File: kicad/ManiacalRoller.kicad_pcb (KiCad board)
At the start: 2 copper layers, 69.5 x 71 mm, 37 parts, among them CON1 AVR-ISP-6, IC1 ATMEGA328P-P, Q1 Q_NPN_EBC, Q2 Q_NPN_EBC, SW1 BTN_coin, SW2 BTN_d4, SW3 BTN_d6, SW4 BTN_d8, SW5 BTN_d10, SW6 BTN_d12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

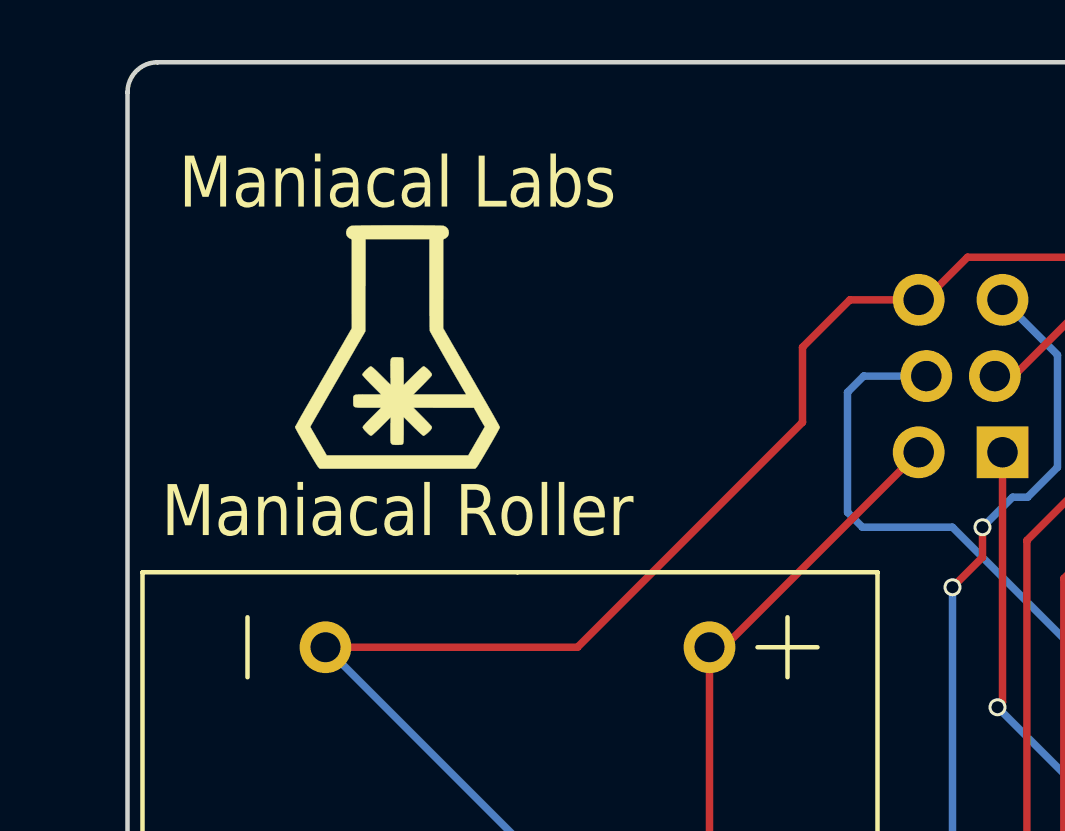
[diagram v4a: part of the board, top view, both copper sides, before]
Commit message: Tweaked logo size/position
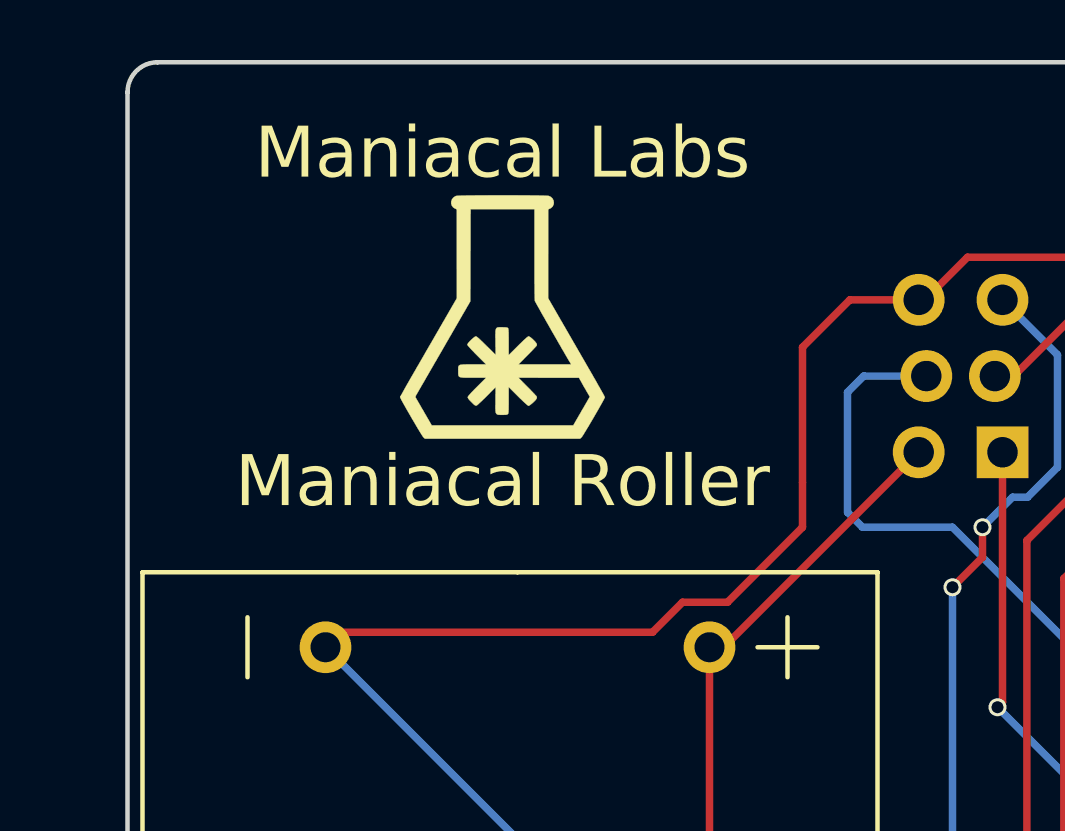
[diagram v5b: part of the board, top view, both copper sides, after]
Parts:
- moved G*** 3.64 mm to (100.0, 50.0)
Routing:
- net GND: track 245.0 -> 247.0 mm
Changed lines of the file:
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@@
     (thickness 1.6)
     (drawings 19)
-    (tracks 364)
+    (tracks 368)
     (zones 0)
     (modules 37)
@@
   )
   (module mod:logo_MLlabs_small (layer F.Cu)
-    (at 96.5 51)
+    (at 100 50)
     (fp_text reference G*** (at 0 0) (layer F.SilkS) hide
       (effects (font (thickness 0.3)))
@@
   (gr_arc (start 88.5 42.5) (end 87.5 42.5) (angle 90) (layer Edge.Cuts) (width 0.15))
   (gr_arc (start 156 111.5) (end 157 111.5) (angle 90) (layer Edge.Cuts) (width 0.15))
-  (gr_text "Maniacal Labs\n\n\n\nManiacal Roller" (at 96.5 51) (layer F.SilkS)
-    (effects (font (size 1.7 1.5) (thickness 0.3)))
+  (gr_text "Maniacal Labs\n\n\n\nManiacal Roller" (at 100 50) (layer F.SilkS)
+    (effects (font (size 1.7 1.7) (thickness 0.3)))
   )
   (gr_text 100 (at 154.5 84 90) (layer F.SilkS)
@@
   (segment (start 130 107) (end 130 109.5) (width 0.25) (layer B.Cu) (net 1))
   (segment (start 130.38 106.62) (end 130 107) (width 0.25) (layer B.Cu) (net 1))
+  (segment (start 94.6 60.5) (end 105 60.5) (width 0.25) (layer F.Cu) (net 2))
+  (segment (start 105 60.5) (end 106 59.5) (width 0.25) (layer F.Cu) (net 2))
+  (segment (start 106 59.5) (end 107.5 59.5) (width 0.25) (layer F.Cu) (net 2))
+  (segment (start 107.5 59.5) (end 110 57) (width 0.25) (layer F.Cu) (net 2))
+  (segment (start 110 57) (end 110 55.5) (width 0.25) (layer F.Cu) (net 2))
+  (segment (start 111.58 49.42) (end 113.873 49.42) (width 0.25) (layer F.Cu) (net 2))
+  (segment (start 110 51) (end 111.58 49.42) (width 0.25) (layer F.Cu) (net 2))
+  (segment (start 110 55.5) (end 110 51) (width 0.25) (layer F.Cu) (net 2))
+  (segment (start 94.6 60.5) (end 94.1 61) (width 0.25) (layer F.Cu) (net 2))
   (segment (start 120 81.5) (end 119.5 81.5) (width 0.25) (layer B.Cu) (net 2))
   (segment (start 119.5 81.5) (end 118 80) (width 0.25) (layer B.Cu) (net 2))
+  (segment (start 118 80) (end 113.1 80) (width 0.25) (layer B.Cu) (net 2))
   (segment (start 113.1 80) (end 94.1 61) (width 0.25) (layer B.Cu) (net 2))
-  (segment (start 118 80) (end 113.1 80) (width 0.25) (layer B.Cu) (net 2))
   (segment (start 132.5 80) (end 135 80) (width 0.25) (layer B.Cu) (net 2))
   (segment (start 135.26 79.74) (end 135.26 77.12) (width 0.25) (layer F.Cu) (net 2))
@@
   (segment (start 119 48) (end 120.5 46.5) (width 0.25) (layer F.Cu) (net 2))
   (segment (start 115.5 48) (end 119 48) (width 0.25) (layer F.Cu) (net 2))
-  (segment (start 94.1 61) (end 102.5 61) (width 0.25) (layer F.Cu) (net 2))
-  (segment (start 111.58 49.42) (end 113.873 49.42) (width 0.25) (layer F.Cu) (net 2))
-  (segment (start 110 51) (end 111.58 49.42) (width 0.25) (layer F.Cu) (net 2))
-  (segment (start 110 53.5) (end 110 51) (width 0.25) (layer F.Cu) (net 2))
-  (segment (start 102.5 61) (end 110 53.5) (width 0.25) (layer F.Cu) (net 2))
   (segment (start 126.5 97.5) (end 126 97.5) (width 0.25) (layer B.Cu) (net 2))
   (segment (start 126 97.5) (end 125 98.5) (width 0.25) (layer B.Cu) (net 2))

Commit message: Bat Hlder on back
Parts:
- added REF**: MountingHole_3.2mm_M3, Mounting_Holes:MountingHole_3.2mm_M3, F.Cu at (154.0, 44.5)
- added REF**: MountingHole_3.2mm_M3, Mounting_Holes:MountingHole_3.2mm_M3, F.Cu at (115.3, 44.5)
- BT1, G***: moved to B.Cu
- moved G*** 49.8 mm to (149.1, 58.3), turned to 180 degrees
- moved BT1 36.9 mm to (133.7, 68.9)
- moved Q1 12.4 mm to (122.1, 44.9)
- moved Q2 10.0 mm to (130.0, 44.9)
- moved R19 2.31 mm to (143.7, 43.7)
- moved R18 2.30 mm to (143.7, 46.1)
- moved CON1 1.20 mm to (115.2, 54.5)
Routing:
- net GND: track 247.0 -> 224.3 mm
- net VBATT: track 166.0 -> 183.2 mm
- net D1: track 5.89 -> 18.1 mm
- net Net-(Q1-Pad2): track 11.5 -> 22.5 mm
- net Net-(Q2-Pad2): track 5.80 -> 13.8 mm
- net D2: track 4.67 -> 12.6 mm
- net MOSI: track 34.8 -> 30.8 mm
- net RST: track 77.0 -> 78.6 mm
- net TENS: track 46.9 -> 48.2 mm
- net SCK: track 37.6 -> 36.4 mm
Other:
- board size 69.5 x 71 mm -> 44.7 x 71 mm
